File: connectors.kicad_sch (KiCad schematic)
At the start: 24 parts, among them J1 UMPT-02-01-L-RA-WT-M-TR, J10 I²C, J11 I²C, J12 I²C, J13 I²C, J14 I²C, J523 GPIO, J525 PWM 4, J526 PWM 3, J527 PWM 2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

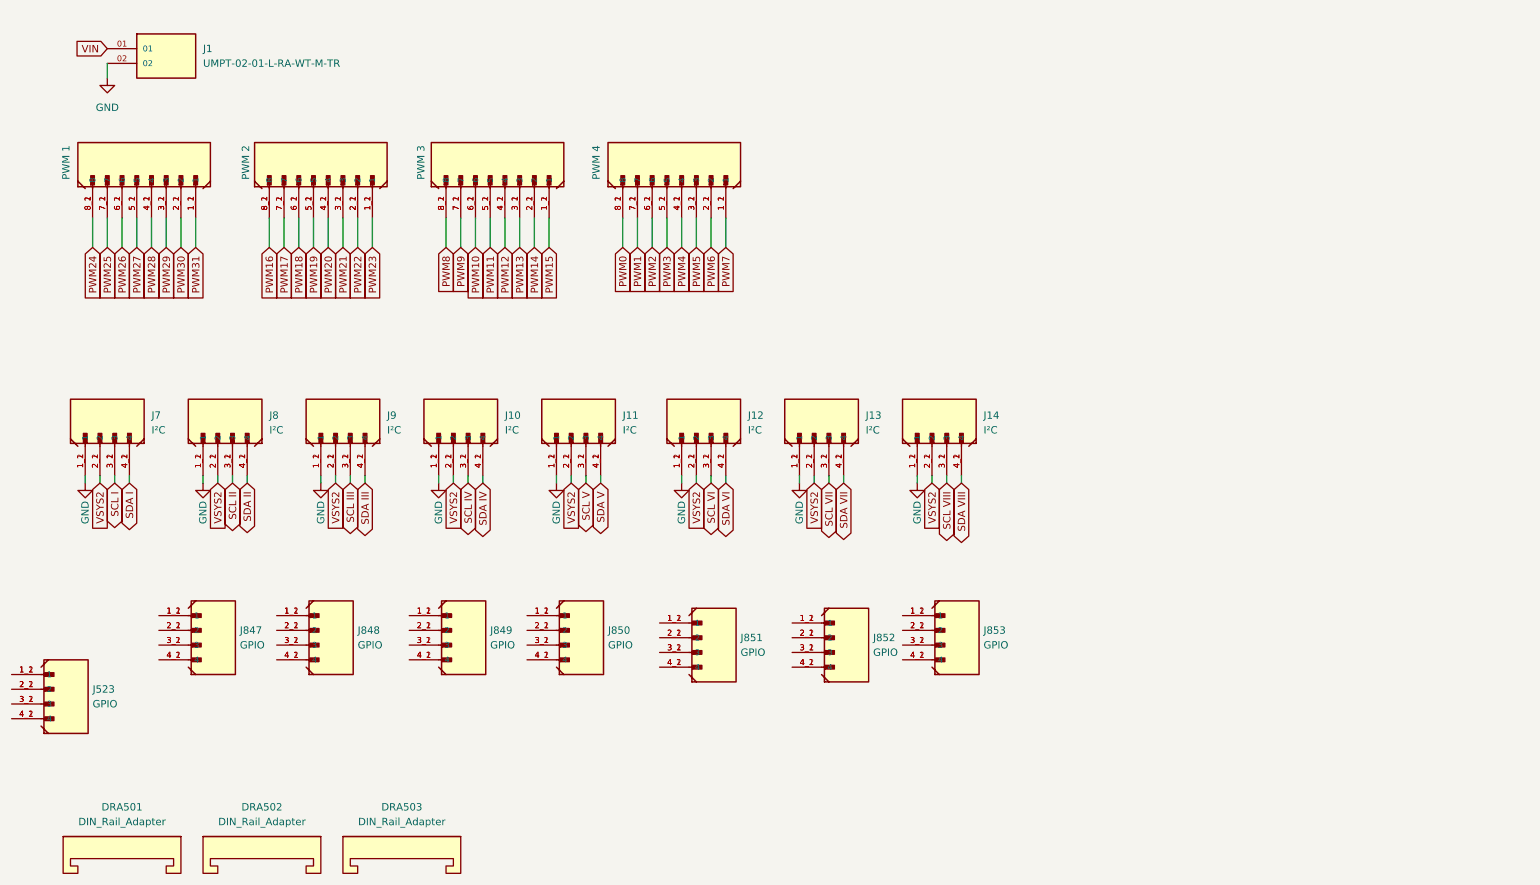
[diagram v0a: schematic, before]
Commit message: Add files via upload
cleaned up, board outline changed, cons cleaned up, 
GPIO now prepped for breakout board.
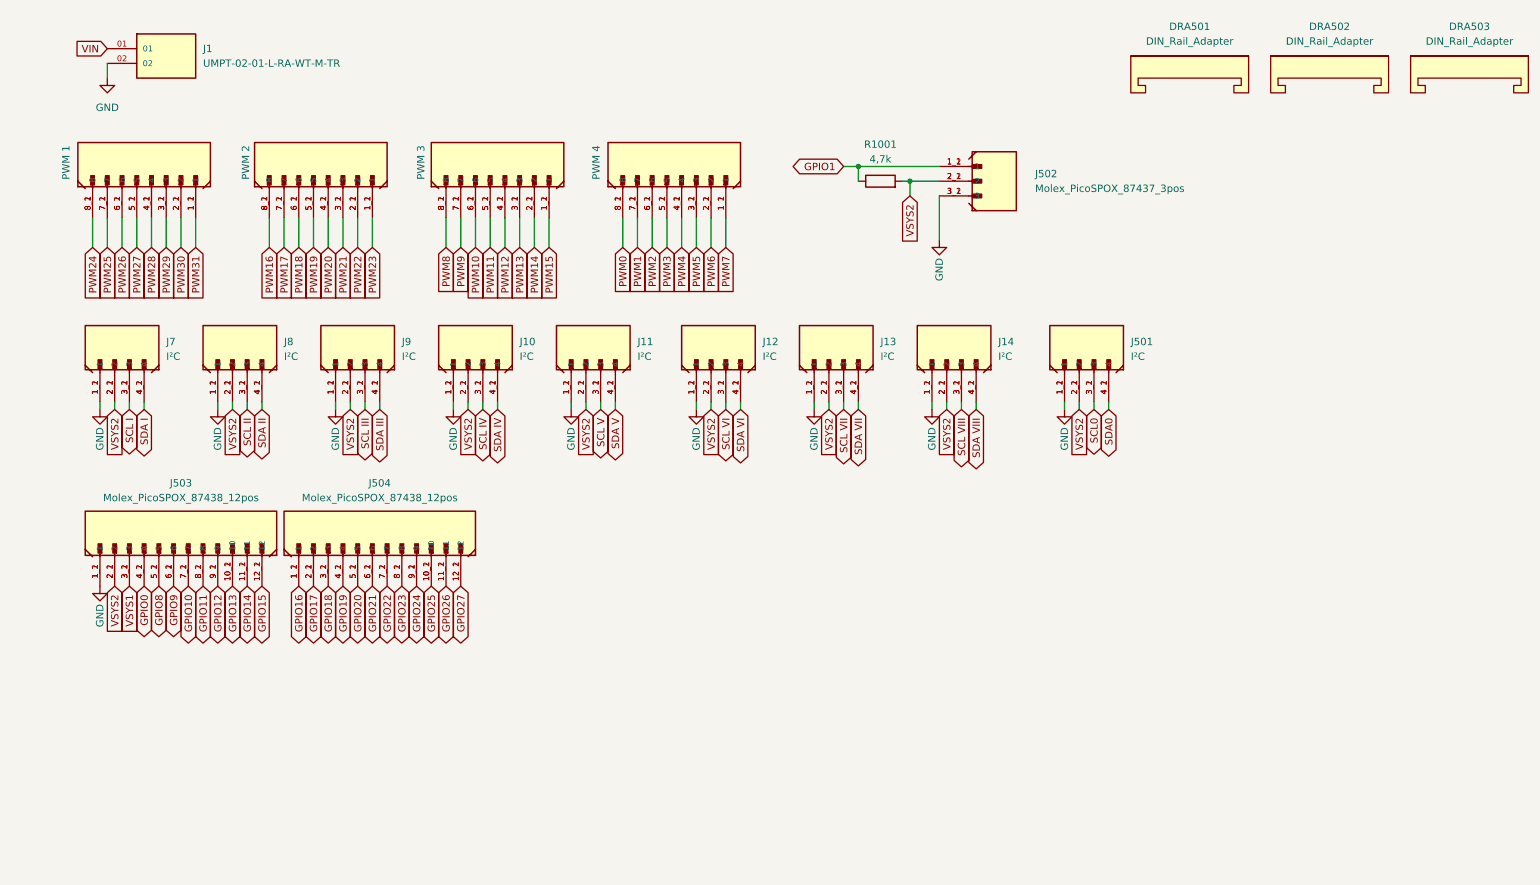
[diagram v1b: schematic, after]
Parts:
- removed J523, J847, J848, J849, J850, J851, J852, J853: GPIO, connectors_molex:MOLEX_874370443, symbol connectors_Molex:Molex_PicoSPOX_87437_4pos
- added J501: I²C, connectors_molex:MOLEX_874370443, symbol connectors_Molex:Molex_PicoSPOX_87438_4pos
- added J502: Molex_PicoSPOX_87437_3pos, connectors_molex:MOLEX_874370343, symbol connectors_Molex:Molex_PicoSPOX_87437_3pos
- added J503, J504: Molex_PicoSPOX_87438_12pos, connectors_molex:MOLEX_874371243, symbol connectors_Molex:Molex_PicoSPOX_87438_12pos
- added R1001: 4,7k, Resistor_SMD:R_0402_1005Metric, symbol Device:R
- J11, J12, J13, J14: footprint connectors_molex:Molex_PicoSpox_hor_4pos_874380443 -> connectors_molex:MOLEX_874370443
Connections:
- net GND: now also J501.1_1 (1), J501.1_2 (1), J502.3_1 (3), J502.3_2 (3), J503.1_1 (1), J503.1_2 (1)
- net VSYS2: now also J501.2_1 (2), J501.2_2 (2), J502.2_1 (2), J502.2_2 (2), J503.2_1 (2), J503.2_2 (2), R1001.2
- new net GPIO0: J503.4_1 (4), J503.4_2 (4)
- new net GPIO1: J502.1_1 (1), J502.1_2 (1), R1001.1
- new net GPIO10: J503.7_1 (7), J503.7_2 (7)
- new net GPIO11: J503.8_1 (8), J503.8_2 (8)
- new net GPIO12: J503.9_1 (9), J503.9_2 (9)
- new net GPIO13: J503.10_1 (10), J503.10_2 (10)
- new net GPIO14: J503.11_1 (11), J503.11_2 (11)
- new net GPIO15: J503.12_1 (12), J503.12_2 (12)
- new net GPIO16: J504.1_1 (1), J504.1_2 (1)
- new net GPIO17: J504.2_1 (2), J504.2_2 (2)
- new net GPIO18: J504.3_1 (3), J504.3_2 (3)
- new net GPIO19: J504.4_1 (4), J504.4_2 (4)
- new net GPIO20: J504.5_1 (5), J504.5_2 (5)
- new net GPIO21: J504.6_1 (6), J504.6_2 (6)
- new net GPIO22: J504.7_1 (7), J504.7_2 (7)
- new net GPIO23: J504.8_1 (8), J504.8_2 (8)
- new net GPIO24: J504.9_1 (9), J504.9_2 (9)
- new net GPIO25: J504.10_1 (10), J504.10_2 (10)
- new net GPIO26: J504.11_1 (11), J504.11_2 (11)
- new net GPIO27: J504.12_1 (12), J504.12_2 (12)
- new net GPIO8: J503.5_1 (5), J503.5_2 (5)
- new net GPIO9: J503.6_1 (6), J503.6_2 (6)
- new net SCL0: J501.3_1 (3), J501.3_2 (3)
- new net SDA0: J501.4_1 (4), J501.4_2 (4)
- new net VSYS1: J503.3_1 (3), J503.3_2 (3)
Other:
- moved on the sheet: DRA501, DRA502, DRA503, J10, J11, J12, J13, J14, J7, J8, J9

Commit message: daughterboard created
divided into mainboard and daughterboard
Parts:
- removed J502: Molex_PicoSPOX_87437_3pos, connectors_molex:MOLEX_874370343, symbol connectors_Molex:Molex_PicoSPOX_87437_3pos
- removed J503, J504: Molex_PicoSPOX_87438_12pos, connectors_molex:MOLEX_874371243, symbol connectors_Molex:Molex_PicoSPOX_87438_12pos
- removed J525: PWM 4, connectors_molex:MOLEX_874370863, symbol connectors_Molex:Molex_PicoSPOX_87438_8pos
- removed J526: PWM 3, connectors_molex:MOLEX_874370863, symbol connectors_Molex:Molex_PicoSPOX_87438_8pos
- removed J527: PWM 2, connectors_molex:MOLEX_874370863, symbol connectors_Molex:Molex_PicoSPOX_87438_8pos
- removed J528: PWM 1, connectors_molex:MOLEX_874370863, symbol connectors_Molex:Molex_PicoSPOX_87438_8pos
- removed R1001: 4,7k, Resistor_SMD:R_0402_1005Metric, symbol Device:R
- J11, J12, J13, J14: footprint connectors_molex:MOLEX_874370443 -> connectors_molex:MOLEX_874380443
- J15: renamed from J501; footprint connectors_molex:MOLEX_874370443 -> connectors_molex:MOLEX_874380443
- J7: footprint connectors_molex:Molex_PicoSpox_hor_4pos_874380443 -> connectors_molex:MOLEX_874380443
- renumbered DRA501 to DRA1, DRA502 to DRA2, DRA503 to DRA3

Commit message: CM4>RP3/4
changed SBC to RP3/4
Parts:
- added H3, H4, H5: MountingHole, MountingHole:MountingHole_2.7mm_M2.5_DIN965, symbol Mechanical:MountingHole
- added J3: Molex_PicoSPOX_87438_3pos, 874380343:MOLEX_874380343, symbol connectors_Molex:Molex_PicoSPOX_87438_3pos
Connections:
- new net: J3.1_1 (1), J3.1_2 (1)
- new net: J3.2_1 (2), J3.2_2 (2)
- new net: J3.3_1 (3), J3.3_2 (3)

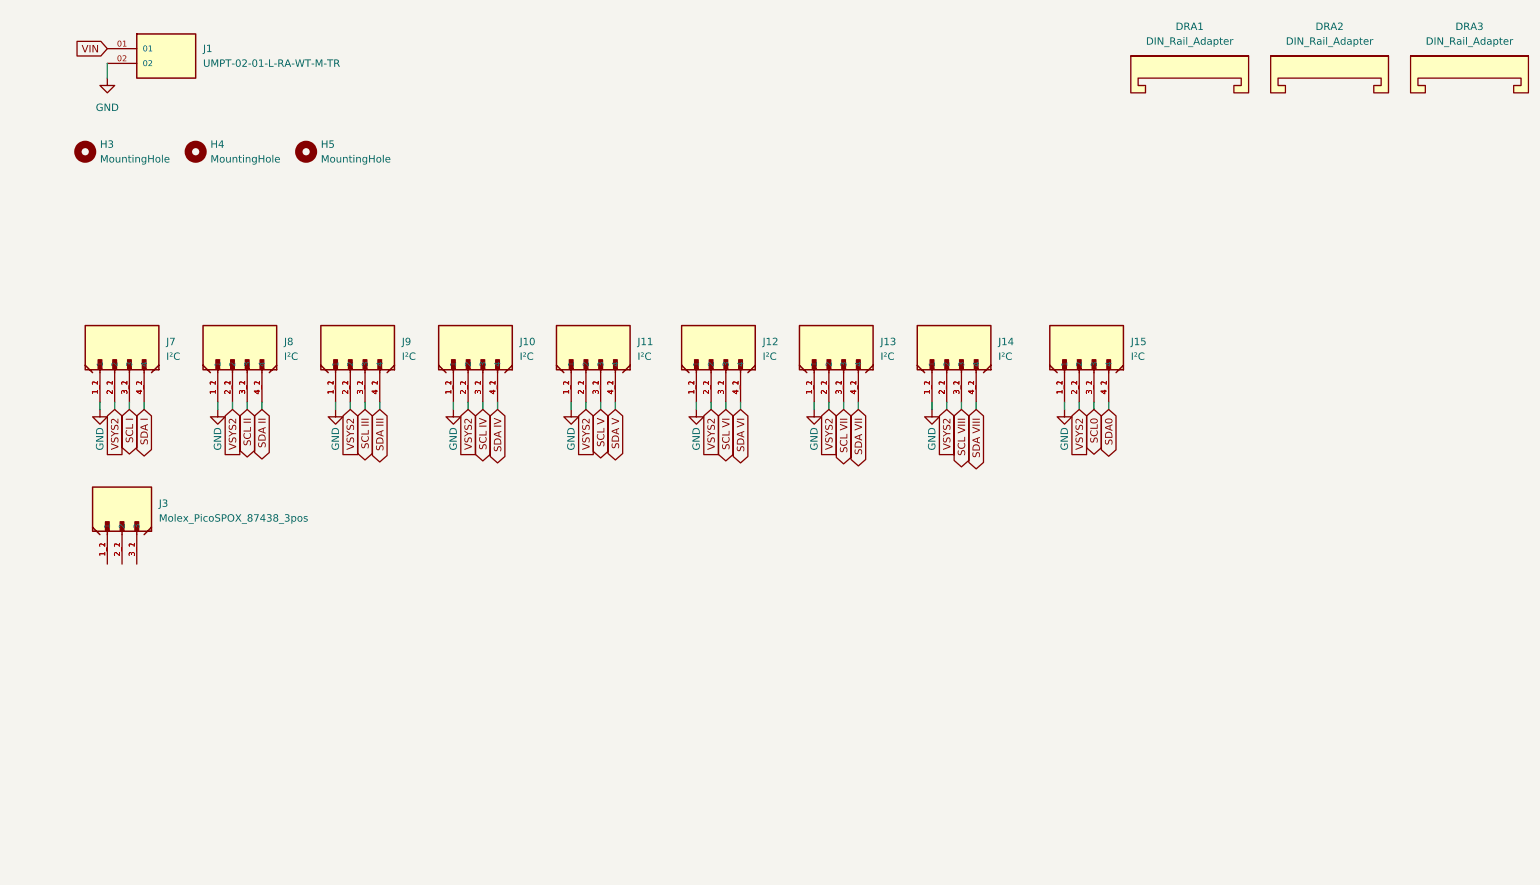
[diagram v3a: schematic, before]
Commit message: prepped for daughterboards
cons and mounting for GPIO-extension, I²C-ports cleaned up
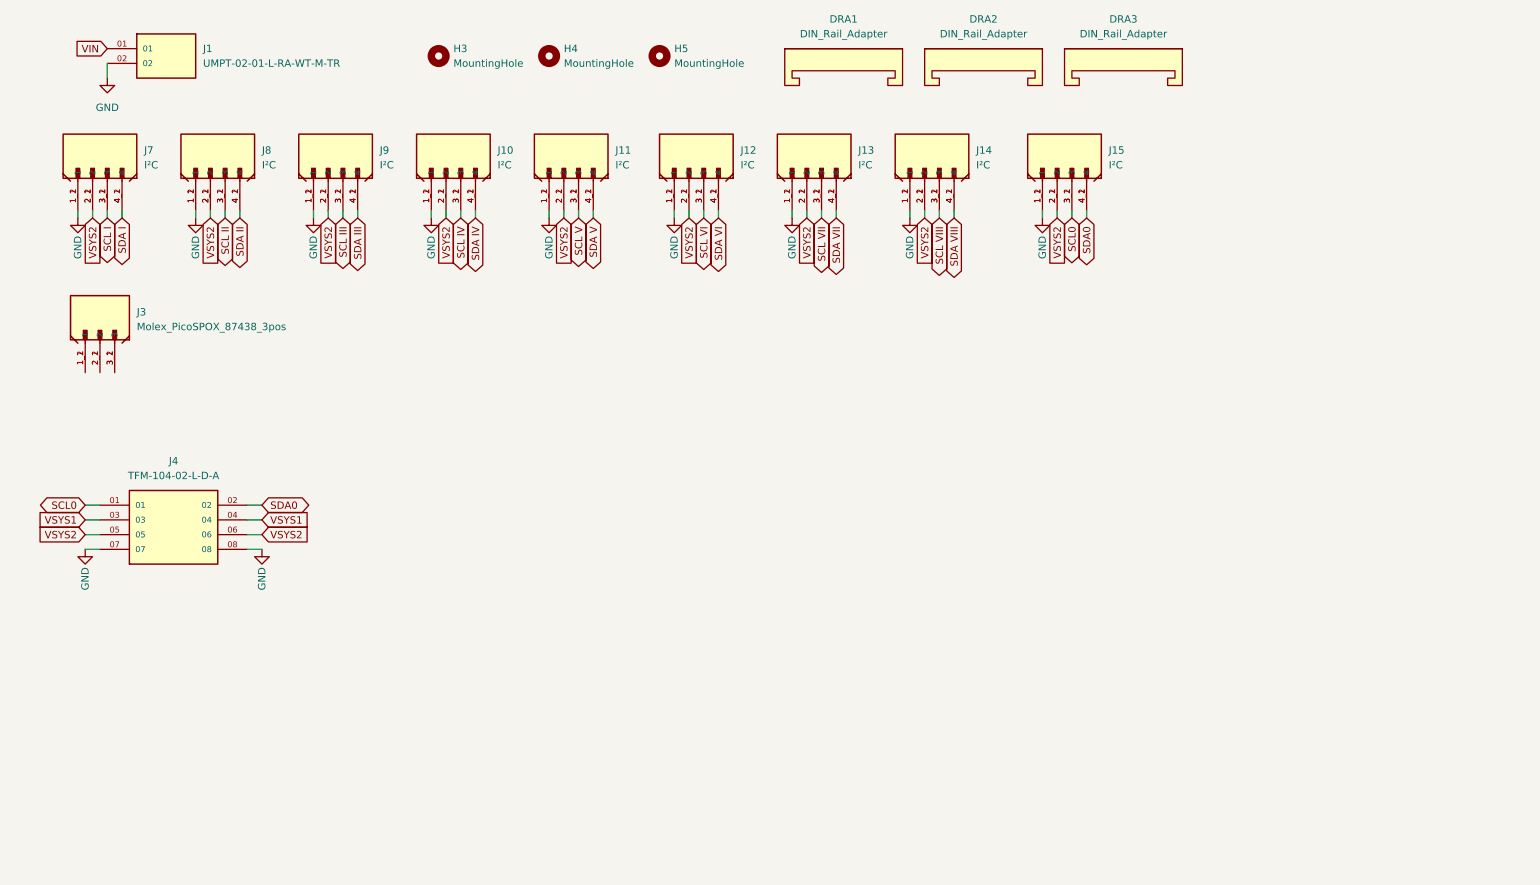
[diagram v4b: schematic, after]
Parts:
- added J4: TFM-104-02-L-D-A, connectors_SAMTEC:SAMTEC_TFM-104-02-L-D-A, symbol connectors_Samtec:TFM-104-02-L-D-A
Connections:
- net GND: now also J4.07, J4.08
- net SCL0: now also J4.01
- net SDA0: now also J4.02
- net VSYS2: now also J4.05, J4.06
- new net VSYS1: J4.03, J4.04
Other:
- moved on the sheet: DRA1, DRA2, DRA3, H3, H4, H5, J10, J11, J12, J13, J14, J15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
